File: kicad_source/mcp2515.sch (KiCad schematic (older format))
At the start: 14 parts, among them CN4 GH_SM04B-GHS-TB, CN5 GH_SM04B-GHS-TB, U4 MCP2515, U8 MCP2515, U9 SN65HVD232, Y1 16MHz

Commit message: exchanged pin D7 and D9 and connected U9, pin8 to GND in readme and schematic as all boards have been reworked
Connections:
- wire segments 80 -> 84
- no-connect marks 2 -> 1
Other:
- note added: "Pin 8 has been connected to GND manually\non all boards to allow usage of SN65HVD230D"
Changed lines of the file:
@@
 TXCAN
 NoConn ~ 9350 2450
-NoConn ~ 9350 2050
 $Comp
 L mechanical-connectors:CONN_01X04 CN?
@@
 Text Notes 7900 6350 0    50   ~ 0
 30V 500mA
+$Comp
+L power-supply:GND #PWR?
+U 1 1 6294B65D
+P 9600 1800
+F 0 "#PWR?" H 9600 1550 50  0001 C CNN
+F 1 "GND" H 9605 1627 50  0000 C CNN
+F 2 "" H 9600 1800 50  0000 C CNN
+F 3 "" H 9600 1800 50  0000 C CNN
+	1    9600 1800
+	1    0    0    -1
+$EndComp
+Wire Wire Line
+	9350 2050 9400 2050
+Wire Wire Line
+	9400 2050 9400 1700
+Wire Wire Line
+	9400 1700 9600 1700
+Wire Wire Line
+	9600 1700 9600 1800
+Text Notes 9000 1500 0    50   ~ 0
+Pin 8 has been connected to GND manually\non all boards to allow usage of SN65HVD230D
 $EndSCHEMATC

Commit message: fixed MCP2515_INT and direction label for Arduino
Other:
- note removed: "Pin 8 has been connected to GND manually\non all boards to allow usage of SN65HVD230D"
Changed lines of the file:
@@
 Sheet 2 3
 Title "l3xz-hw_leg-controller"
-Date "2022-04-12"
-Rev "0.1"
+Date "2022-06-05"
+Rev "dev_0.2"
 Comp "107-systems"
 Comment1 ""
@@
 30V 500mA
 $Comp
-L power-supply:GND #PWR?
+L power-supply:GND #PWR0102
 U 1 1 6294B65D
 P 9600 1800
-F 0 "#PWR?" H 9600 1550 50  0001 C CNN
+F 0 "#PWR0102" H 9600 1550 50  0001 C CNN
 F 1 "GND" H 9605 1627 50  0000 C CNN
 F 2 "" H 9600 1800 50  0000 C CNN
@@
 Wire Wire Line
 	9600 1700 9600 1800
-Text Notes 9000 1500 0    50   ~ 0
-Pin 8 has been connected to GND manually\non all boards to allow usage of SN65HVD230D
 $EndSCHEMATC

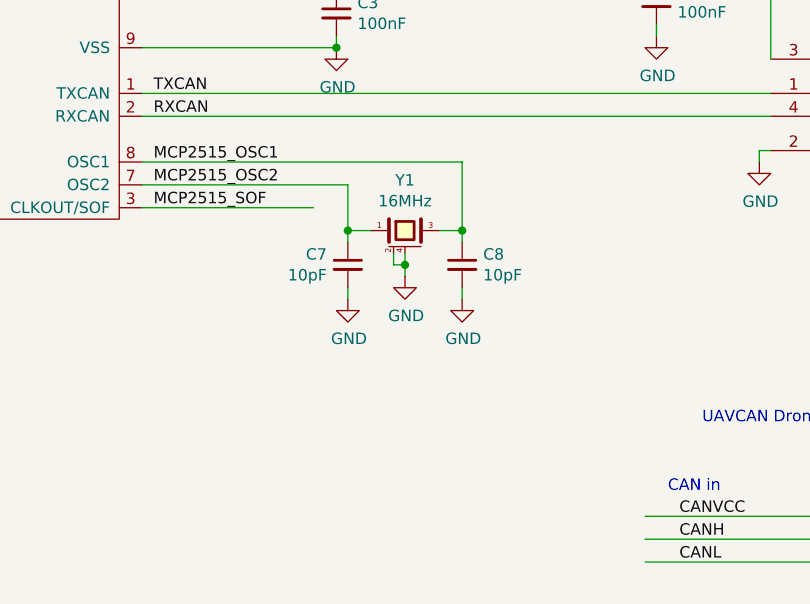
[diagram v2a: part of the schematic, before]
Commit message: fixed crystal issues, corrected CAN driver footprint, added pullup on MISO
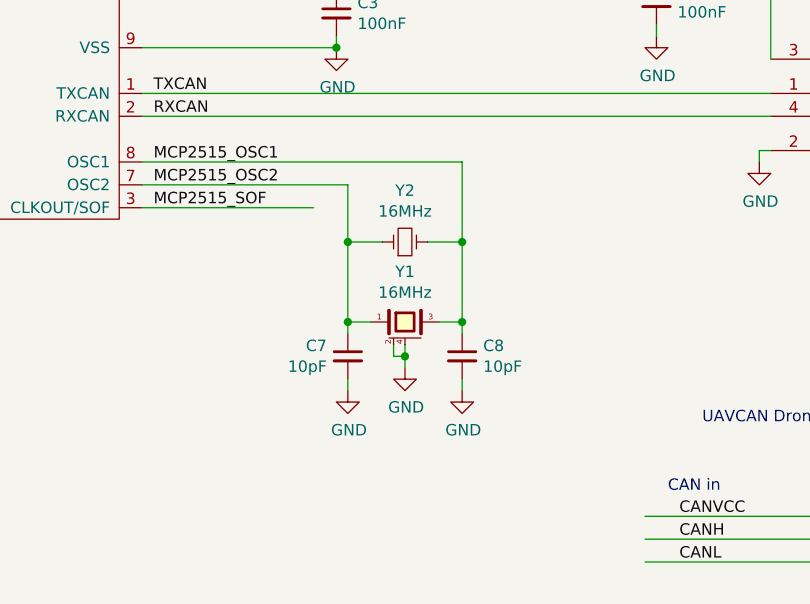
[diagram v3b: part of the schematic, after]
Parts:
- added Y2: 16MHz, crystals:HC-49V, symbol devices:Crystal_Small
- U9: footprint SOIC:SOIJ-8_5.3x5.3mm_Pitch1.27mm -> SOIC:SOIC-8_3.9x4.9mm_Pitch1.27mm
- Y1: footprint crystals:Crystal_SMD_0603_4Pads -> crystals:Crystal_SMD_3.2x2.5mm_4Pad
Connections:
- wire segments 84 -> 88
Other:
- moved on the sheet: C7, C8, Y1
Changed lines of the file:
@@
 L devices:Crystal_SMD_4Pad Y1
 U 1 1 5ED95D76
-P 6700 2800
-F 0 "Y1" H 6700 3020 50  0000 C CNN
-F 1 "16MHz" H 6700 2929 50  0000 C CNN
-F 2 "crystals:Crystal_SMD_0603_4Pads" H 6700 2600 50  0001 C CNN
-F 3 "" H 6700 2800 50  0000 C CNN
-	1    6700 2800
+P 6700 3200
+F 0 "Y1" H 6700 3420 50  0000 C CNN
+F 1 "16MHz" H 6700 3329 50  0000 C CNN
+F 2 "crystals:Crystal_SMD_3.2x2.5mm_4Pad" H 6700 3000 50  0001 C CNN
+F 3 "" H 6700 3200 50  0000 C CNN
+	1    6700 3200
 	1    0    0    -1
 $EndComp
@@
 L power-supply:GND #PWR027
 U 1 1 5ED9771C
-P 6700 3000
-F 0 "#PWR027" H 6700 2750 50  0001 C CNN
-F 1 "GND" H 6705 2827 50  0000 C CNN
-F 2 "" H 6700 3000 50  0000 C CNN
-F 3 "" H 6700 3000 50  0000 C CNN
-	1    6700 3000
-	1    0    0    -1
-$EndComp
-Wire Wire Line
-	6950 2500 6950 2800
-Wire Wire Line
-	6950 2800 6850 2800
-Wire Wire Line
-	6450 2600 6450 2800
-Wire Wire Line
-	6450 2800 6550 2800
-Wire Wire Line
-	6700 2900 6700 2950
-Wire Wire Line
-	6650 2900 6650 2950
-Wire Wire Line
-	6650 2950 6700 2950
-Connection ~ 6700 2950
-Wire Wire Line
-	6700 2950 6700 3000
+P 6700 3400
+F 0 "#PWR027" H 6700 3150 50  0001 C CNN
+F 1 "GND" H 6705 3227 50  0000 C CNN
+F 2 "" H 6700 3400 50  0000 C CNN
+F 3 "" H 6700 3400 50  0000 C CNN
+	1    6700 3400
+	1    0    0    -1
+$EndComp
+Wire Wire Line
+	6950 3200 6850 3200
+Wire Wire Line
+	6450 3200 6550 3200
+Wire Wire Line
+	6700 3300 6700 3350
+Wire Wire Line
+	6650 3300 6650 3350
+Wire Wire Line
+	6650 3350 6700 3350
+Connection ~ 6700 3350
+Wire Wire Line
+	6700 3350 6700 3400
 $Comp
 L devices:R_0603 R3
@@
 F 0 "U9" H 8825 3487 60  0000 C CNN
 F 1 "SN65HVD232" H 8825 3381 60  0000 C CNN
-F 2 "SOIC:SOIJ-8_5.3x5.3mm_Pitch1.27mm" H 9150 2550 60  0001 C CNN
+F 2 "SOIC:SOIC-8_3.9x4.9mm_Pitch1.27mm" H 9150 2550 60  0001 C CNN
 F 3 "" H 8300 2750 60  0000 C CNN
 	1    8300 2600
@@
 L devices:C_0603 C8
 U 1 1 62513A43
-P 6950 2950
-F 0 "C8" H 7042 2996 50  0000 L CNN
-F 1 "10pF" H 7042 2905 50  0000 L CNN
-F 2 "capacitors:C_0603" H 6950 2800 50  0001 C CNN
-F 3 "" H 6950 2950 50  0000 C CNN
-	1    6950 2950
+P 6950 3350
+F 0 "C8" H 7042 3396 50  0000 L CNN
+F 1 "10pF" H 7042 3305 50  0000 L CNN
+F 2 "capacitors:C_0603" H 6950 3200 50  0001 C CNN
+F 3 "" H 6950 3350 50  0000 C CNN
+	1    6950 3350
 	1    0    0    -1
 $EndComp
@@
 L devices:C_0603 C7
 U 1 1 6251419A
-P 6450 2950
-F 0 "C7" H 6542 2996 50  0000 L CNN
-F 1 "10pF" H 6542 2905 50  0000 L CNN
-F 2 "capacitors:C_0603" H 6450 2800 50  0001 C CNN
-F 3 "" H 6450 2950 50  0000 C CNN
-	1    6450 2950
+P 6450 3350
+F 0 "C7" H 6542 3396 50  0000 L CNN
+F 1 "10pF" H 6542 3305 50  0000 L CNN
+F 2 "capacitors:C_0603" H 6450 3200 50  0001 C CNN
+F 3 "" H 6450 3350 50  0000 C CNN
+	1    6450 3350
 	-1   0    0    -1
 $EndComp
@@
 L power-supply:GND #PWR034
 U 1 1 625148D1
-P 6450 3100
-F 0 "#PWR034" H 6450 2850 50  0001 C CNN
-F 1 "GND" H 6455 2927 50  0000 C CNN
-F 2 "" H 6450 3100 50  0000 C CNN
-F 3 "" H 6450 3100 50  0000 C CNN
-	1    6450 3100
+P 6450 3500
+F 0 "#PWR034" H 6450 3250 50  0001 C CNN
+F 1 "GND" H 6455 3327 50  0000 C CNN
+F 2 "" H 6450 3500 50  0000 C CNN
+F 3 "" H 6450 3500 50  0000 C CNN
+	1    6450 3500
 	1    0    0    -1
 $EndComp
@@
 L power-supply:GND #PWR035
 U 1 1 62514AF6
-P 6950 3100
-F 0 "#PWR035" H 6950 2850 50  0001 C CNN
-F 1 "GND" H 6955 2927 50  0000 C CNN
-F 2 "" H 6950 3100 50  0000 C CNN
-F 3 "" H 6950 3100 50  0000 C CNN
-	1    6950 3100
-	1    0    0    -1
-$EndComp
-Wire Wire Line
-	6450 2850 6450 2800
-Connection ~ 6450 2800
-Wire Wire Line
-	6950 2850 6950 2800
-Connection ~ 6950 2800
-Wire Wire Line
-	6950 3050 6950 3100
-Wire Wire Line
-	6450 3050 6450 3100
+P 6950 3500
+F 0 "#PWR035" H 6950 3250 50  0001 C CNN
+F 1 "GND" H 6955 3327 50  0000 C CNN
+F 2 "" H 6950 3500 50  0000 C CNN
+F 3 "" H 6950 3500 50  0000 C CNN
+	1    6950 3500
+	1    0    0    -1
+$EndComp
+Wire Wire Line
+	6450 3250 6450 3200
+Connection ~ 6450 3200
+Wire Wire Line
+	6950 3250 6950 3200
+Connection ~ 6950 3200
+Wire Wire Line
+	6950 3450 6950 3500
+Wire Wire Line
+	6450 3450 6450 3500
 $Comp
 L power-supply:+BATT #PWR038
@@
 Wire Wire Line
 	9600 1700 9600 1800
+Wire Wire Line
+	6450 2600 6450 2850
+Wire Wire Line
+	6950 2500 6950 2850
+$Comp
+L devices:Crystal_Small Y2
+U 1 1 629E5265
+P 6700 2850
+F 0 "Y2" H 6700 3075 50  0000 C CNN
+F 1 "16MHz" H 6700 2984 50  0000 C CNN
+F 2 "crystals:HC-49V" H 6700 2850 50  0001 C CNN
+F 3 "" H 6700 2850 50  0000 C CNN
+	1    6700 2850
+	1    0    0    -1
+$EndComp
+Wire Wire Line
+	6800 2850 6950 2850
+Connection ~ 6950 2850
+Wire Wire Line
+	6950 2850 6950 3200
+Wire Wire Line
+	6600 2850 6450 2850
+Connection ~ 6450 2850
+Wire Wire Line
+	6450 2850 6450 3200
 $EndSCHEMATC

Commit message: updated images and schematic pdf
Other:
- note added: "UCANPHY Micro connectors"
- note added: "connect pin to GND\nto allow usage of SN65HVD230"
- note removed: "UAVCAN Dronecode connectors"
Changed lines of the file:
@@
 CAN in
 Text Notes 8000 3650 0    50   ~ 0
-UAVCAN Dronecode connectors
+UCANPHY Micro connectors
 $Comp
 L mechanical-connectors:CONN_01X04 CN?
@@
 Wire Wire Line
 	8800 6150 8100 6150
-Wire Wire Line
-	7900 6150 7750 6150
-Wire Wire Line
-	7750 6150 7750 6100
 Text Label 7900 5000 0    50   ~ 0
 CANVCC
@@
 L power-supply:+BATT #PWR038
 U 1 1 6252FED9
-P 7750 6100
-F 0 "#PWR038" H 7750 5950 50  0001 C CNN
-F 1 "+BATT" H 7765 6273 50  0000 C CNN
-F 2 "" H 7750 6100 50  0000 C CNN
-F 3 "" H 7750 6100 50  0000 C CNN
-	1    7750 6100
+P 7700 6100
+F 0 "#PWR038" H 7700 5950 50  0001 C CNN
+F 1 "+BATT" H 7715 6273 50  0000 C CNN
+F 2 "" H 7700 6100 50  0000 C CNN
+F 3 "" H 7700 6100 50  0000 C CNN
+	1    7700 6100
 	1    0    0    -1
 $EndComp
@@
 Wire Wire Line
 	6450 2850 6450 3200
+Text Notes 8950 1450 0    50   ~ 0
+connect pin to GND\nto allow usage of SN65HVD230
+Wire Wire Line
+	7700 6150 7700 6100
+Wire Wire Line
+	7700 6150 7900 6150
 $EndSCHEMATC
